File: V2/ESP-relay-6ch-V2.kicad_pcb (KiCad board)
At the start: 2 copper layers, 173 x 67.8 mm, 111 parts, among them J1 POWER & INPUTS, J2 OUT1, J3 OUT1, J4 OUT1, J5 OUT1, J6 OUT1, J7 OUT1, K1 G5PZ-1A, K2 G5PZ-1A, K3 G5PZ-1A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

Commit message: pcb tweaks
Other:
- board text added: "ESP-RELAY-6CH-V2"
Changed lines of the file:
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@@
     (effects (font (size 1.5 1.3) (thickness 0.2)))
+  )
+  (gr_text "ESP-RELAY-6CH-V2" (at 133.35 115.57) (layer "F.SilkS")
+    (effects (font (size 1.2 1.2) (thickness 0.2)))
   )
   (gr_text "MAX LOAD 10A/CHANNEL" (at 133.35 129.54) (layer "F.SilkS")

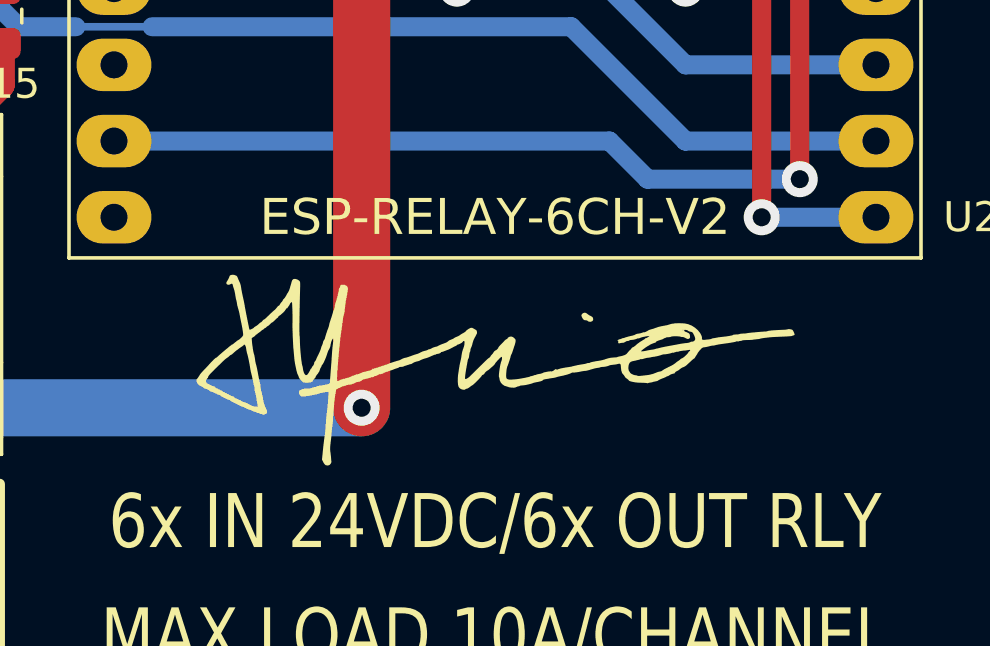
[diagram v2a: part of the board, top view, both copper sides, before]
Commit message: Update ESP-relay-6ch-V2.kicad_pcb
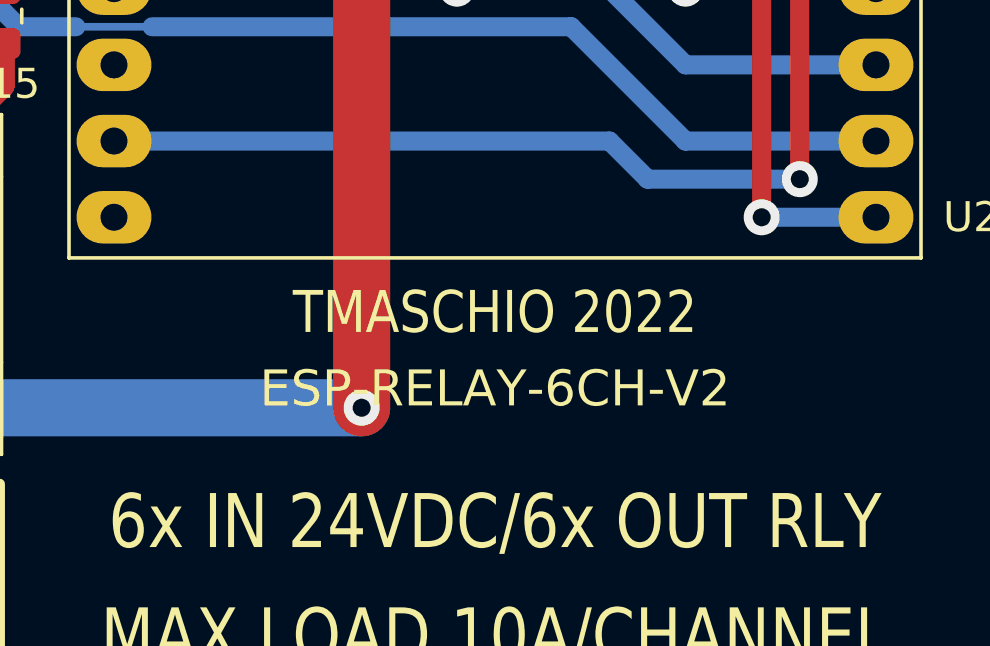
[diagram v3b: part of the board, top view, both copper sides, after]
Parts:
- removed ?: , Tales:TMaschio_20x6.4mm
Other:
- board text added: "TMASCHIO 2022"
